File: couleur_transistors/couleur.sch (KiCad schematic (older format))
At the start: 20 parts, among them P1 CONN_02X03, P2 Mounting, P3 Mounting, P4 Mounting, P5 Mounting, U1 S4282-51

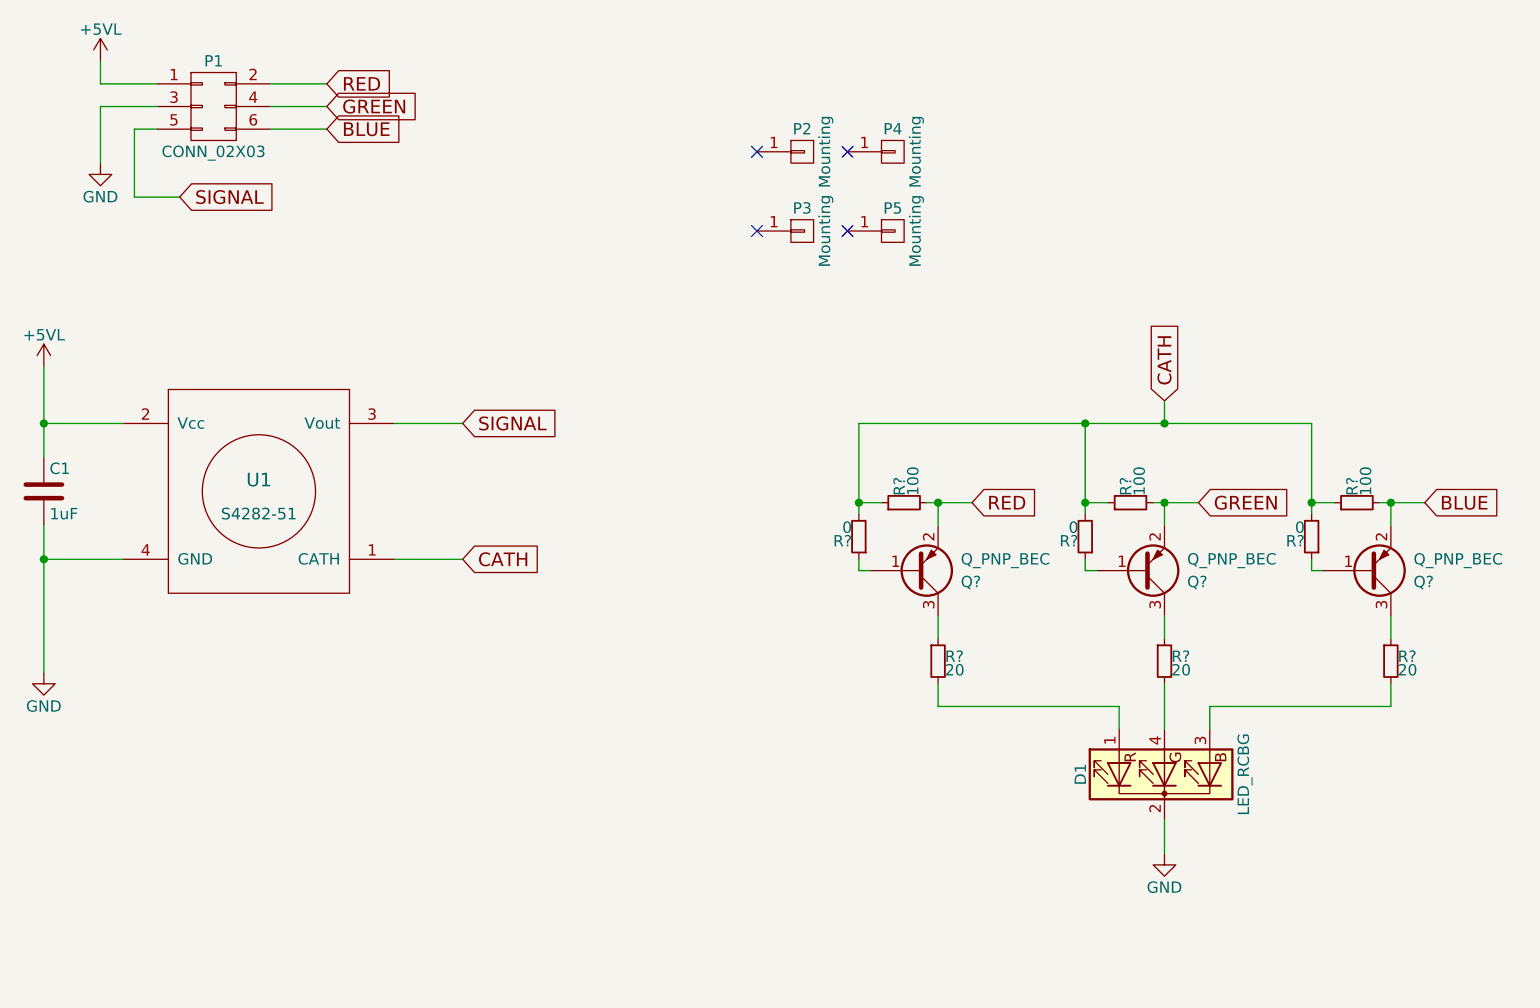
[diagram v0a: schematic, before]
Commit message: COuleur avec transistors
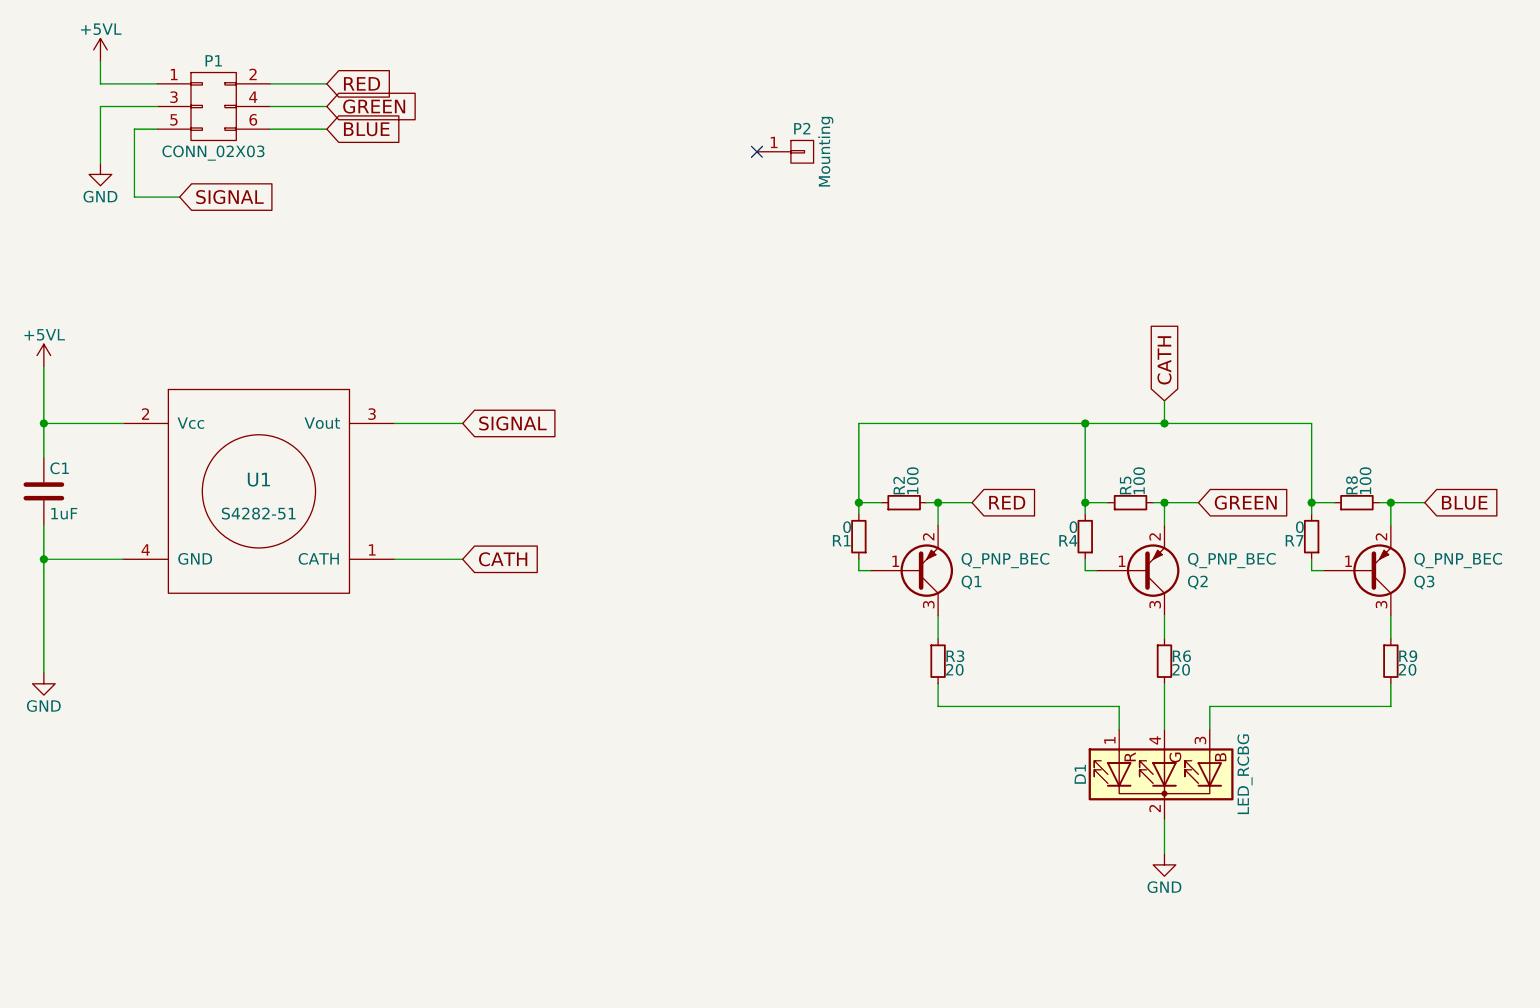
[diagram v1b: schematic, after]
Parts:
- removed P3, P4, P5: Mounting, Mounting_Holes:MountingHole_3.2mm_M3_Pad, symbol CONN_01X01
- Q1, Q2, Q3: renamed from Q?; footprint (none) -> TO_SOT_Packages_SMD:SOT-23
- R1, R2, R3, R4, R5, R6, R7, R8, R9: renamed from R?; footprint (none) -> Resistors_SMD:R_0603_HandSoldering
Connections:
- no-connect marks 4 -> 1
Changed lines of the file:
@@
 $EndComp
 $Comp
-L GND #PWR2
+L GND #PWR01
 U 1 1 5A77312B
 P 3550 4800
-F 0 "#PWR2" H 3550 4550 50  0001 C CNN
+F 0 "#PWR01" H 3550 4550 50  0001 C CNN
 F 1 "GND" H 3550 4650 50  0000 C CNN
 F 2 "" H 3550 4800 50  0000 C CNN
@@
 $EndComp
 $Comp
-L +5VL #PWR1
+L +5VL #PWR02
 U 1 1 5A773143
 P 3550 3450
-F 0 "#PWR1" H 3550 3300 50  0001 C CNN
+F 0 "#PWR02" H 3550 3300 50  0001 C CNN
 F 1 "+5VL" H 3550 3590 50  0000 C CNN
 F 2 "" H 3550 3450 50  0000 C CNN
@@
 $EndComp
 Wire Wire Line
-	3550 3450 3550 3700
-Wire Wire Line
-	3550 3700 3550 3850
+	3550 3450 3550 3850
 Wire Wire Line
 	3550 3700 3900 3700
@@
 	3900 4300 3550 4300
 Wire Wire Line
-	3550 4150 3550 4300
-Wire Wire Line
-	3550 4300 3550 4800
-$Comp
-L +5VL #PWR3
+	3550 4150 3550 4800
+$Comp
+L +5VL #PWR03
 U 1 1 5A773165
 P 3800 2100
-F 0 "#PWR3" H 3800 1950 50  0001 C CNN
+F 0 "#PWR03" H 3800 1950 50  0001 C CNN
 F 1 "+5VL" H 3800 2240 50  0000 C CNN
 F 2 "" H 3800 2100 50  0000 C CNN
@@
 $EndComp
 $Comp
-L GND #PWR4
+L GND #PWR04
 U 1 1 5A773176
 P 3800 2550
-F 0 "#PWR4" H 3800 2300 50  0001 C CNN
+F 0 "#PWR04" H 3800 2300 50  0001 C CNN
 F 1 "GND" H 3800 2400 50  0000 C CNN
 F 2 "" H 3800 2550 50  0000 C CNN
@@
 $EndComp
 NoConn ~ 6700 2500
-$Comp
-L CONN_01X01 P3
-U 1 1 5A7B0BC5
-P 6900 2850
-F 0 "P3" H 6900 2950 50  0000 C CNN
-F 1 "Mounting" V 7000 2850 50  0000 C CNN
-F 2 "Mounting_Holes:MountingHole_3.2mm_M3_Pad" H 6900 2850 50  0001 C CNN
-F 3 "" H 6900 2850 50  0000 C CNN
-	1    6900 2850
-	1    0    0    -1
-$EndComp
-NoConn ~ 6700 2850
-$Comp
-L CONN_01X01 P4
-U 1 1 5A7B0C29
-P 7300 2500
-F 0 "P4" H 7300 2600 50  0000 C CNN
-F 1 "Mounting" V 7400 2500 50  0000 C CNN
-F 2 "Mounting_Holes:MountingHole_3.2mm_M3_Pad" H 7300 2500 50  0001 C CNN
-F 3 "" H 7300 2500 50  0000 C CNN
-	1    7300 2500
-	1    0    0    -1
-$EndComp
-$Comp
-L CONN_01X01 P5
-U 1 1 5A7B0CFA
-P 7300 2850
-F 0 "P5" H 7300 2950 50  0000 C CNN
-F 1 "Mounting" V 7400 2850 50  0000 C CNN
-F 2 "Mounting_Holes:MountingHole_3.2mm_M3_Pad" H 7300 2850 50  0001 C CNN
-F 3 "" H 7300 2850 50  0000 C CNN
-	1    7300 2850
-	1    0    0    -1
-$EndComp
-NoConn ~ 7100 2500
-NoConn ~ 7100 2850
 $Comp
 L LED_RCBG D1
@@
 $EndComp
 $Comp
-L GND #PWR?
+L GND #PWR05
 U 1 1 5A7A0A21
 P 8500 5600
-F 0 "#PWR?" H 8500 5350 50  0001 C CNN
+F 0 "#PWR05" H 8500 5350 50  0001 C CNN
 F 1 "GND" H 8500 5450 50  0000 C CNN
 F 2 "" H 8500 5600 50  0000 C CNN
@@
 	8500 5450 8500 5600
 $Comp
-L Q_PNP_BEC Q?
+L Q_PNP_BEC Q1
 U 1 1 5A7A0A6A
 P 7400 4350
-F 0 "Q?" H 7600 4400 50  0000 L CNN
+F 0 "Q1" H 7600 4400 50  0000 L CNN
 F 1 "Q_PNP_BEC" H 7600 4300 50  0000 L CNN
-F 2 "" H 7600 4450 50  0000 C CNN
+F 2 "TO_SOT_Packages_SMD:SOT-23" H 7600 4450 50  0001 C CNN
 F 3 "" H 7400 4350 50  0000 C CNN
 	1    7400 4350
@@
 $EndComp
 $Comp
-L R_Small R?
+L R_Small R3
 U 1 1 5A7A0C40
 P 7500 4750
-F 0 "R?" H 7530 4770 50  0000 L CNN
+F 0 "R3" H 7530 4770 50  0000 L CNN
 F 1 "20" H 7530 4710 50  0000 L CNN
-F 2 "" H 7500 4750 50  0000 C CNN
+F 2 "Resistors_SMD:R_0603_HandSoldering" H 7500 4750 50  0001 C CNN
 F 3 "" H 7500 4750 50  0000 C CNN
 	1    7500 4750
@@
 $EndComp
 $Comp
-L R_Small R?
+L R_Small R6
 U 1 1 5A7A0C7B
 P 8500 4750
-F 0 "R?" H 8530 4770 50  0000 L CNN
+F 0 "R6" H 8530 4770 50  0000 L CNN
 F 1 "20" H 8530 4710 50  0000 L CNN
-F 2 "" H 8500 4750 50  0000 C CNN
+F 2 "Resistors_SMD:R_0603_HandSoldering" H 8500 4750 50  0001 C CNN
 F 3 "" H 8500 4750 50  0000 C CNN
 	1    8500 4750
@@
 $EndComp
 $Comp
-L R_Small R?
+L R_Small R9
 U 1 1 5A7A0CB2
 P 9500 4750
-F 0 "R?" H 9530 4770 50  0000 L CNN
+F 0 "R9" H 9530 4770 50  0000 L CNN
 F 1 "20" H 9530 4710 50  0000 L CNN
-F 2 "" H 9500 4750 50  0000 C CNN
+F 2 "Resistors_SMD:R_0603_HandSoldering" H 9500 4750 50  0001 C CNN
 F 3 "" H 9500 4750 50  0000 C CNN
 	1    9500 4750
@@
 $EndComp
 $Comp
-L R_Small R?
+L R_Small R1
 U 1 1 5A7A0CF2
 P 7150 4200
-F 0 "R?" H 7180 4220 50  0000 L CNN
+F 0 "R1" H 7180 4220 50  0000 L CNN
 F 1 "0" H 7180 4160 50  0000 L CNN
-F 2 "" H 7150 4200 50  0000 C CNN
+F 2 "Resistors_SMD:R_0603_HandSoldering" H 7150 4200 50  0001 C CNN
 F 3 "" H 7150 4200 50  0000 C CNN
 	1    7150 4200
@@
 $EndComp
 $Comp
-L R_Small R?
+L R_Small R2
 U 1 1 5A7A0D69
 P 7350 4050
-F 0 "R?" H 7380 4070 50  0000 L CNN
+F 0 "R2" H 7380 4070 50  0000 L CNN
 F 1 "100" H 7380 4010 50  0000 L CNN
-F 2 "" H 7350 4050 50  0000 C CNN
+F 2 "Resistors_SMD:R_0603_HandSoldering" H 7350 4050 50  0001 C CNN
 F 3 "" H 7350 4050 50  0000 C CNN
 	1    7350 4050
@@
 	7500 4150 7500 4050
 Wire Wire Line
-	7450 4050 7500 4050
-Wire Wire Line
-	7500 4050 7650 4050
+	7450 4050 7650 4050
 Wire Wire Line
 	7250 4050 7150 4050
@@
 CATH
 $Comp
-L R_Small R?
+L R_Small R4
 U 1 1 5A7A1702
 P 8150 4200
-F 0 "R?" H 8180 4220 50  0000 L CNN
+F 0 "R4" H 8180 4220 50  0000 L CNN
 F 1 "0" H 8180 4160 50  0000 L CNN
-F 2 "" H 8150 4200 50  0000 C CNN
+F 2 "Resistors_SMD:R_0603_HandSoldering" H 8150 4200 50  0001 C CNN
 F 3 "" H 8150 4200 50  0000 C CNN
 	1    8150 4200
@@
 $EndComp
 Wire Wire Line
-	8150 3700 8150 4050
-Wire Wire Line
-	8150 4050 8150 4100
-$Comp
-L R_Small R?
+	8150 3700 8150 4100
+$Comp
+L R_Small R5
 U 1 1 5A7A184F
 P 8350 4050
-F 0 "R?" H 8380 4070 50  0000 L CNN
+F 0 "R5" H 8380 4070 50  0000 L CNN
 F 1 "100" H 8380 4010 50  0000 L CNN
-F 2 "" H 8350 4050 50  0000 C CNN
+F 2 "Resistors_SMD:R_0603_HandSoldering" H 8350 4050 50  0001 C CNN
 F 3 "" H 8350 4050 50  0000 C CNN
 	1    8350 4050
@@
 Connection ~ 8150 4050
 $Comp
-L Q_PNP_BEC Q?
+L Q_PNP_BEC Q2
 U 1 1 5A7A18E8
 P 8400 4350
-F 0 "Q?" H 8600 4400 50  0000 L CNN
+F 0 "Q2" H 8600 4400 50  0000 L CNN
 F 1 "Q_PNP_BEC" H 8600 4300 50  0000 L CNN
-F 2 "" H 8600 4450 50  0000 C CNN
+F 2 "TO_SOT_Packages_SMD:SOT-23" H 8600 4450 50  0001 C CNN
 F 3 "" H 8400 4350 50  0000 C CNN
 	1    8400 4350
@@
 	8150 4350 8200 4350
 Wire Wire Line
-	8450 4050 8500 4050
-Wire Wire Line
-	8500 4050 8650 4050
+	8450 4050 8650 4050
 Wire Wire Line
 	8500 4050 8500 4150
@@
 	8500 4550 8500 4650
 Wire Wire Line
-	7150 3700 7150 4050
-Wire Wire Line
-	7150 4050 7150 4100
-Wire Wire Line
-	7150 3700 8150 3700
-Wire Wire Line
-	8150 3700 8500 3700
-Wire Wire Line
-	8500 3700 9150 3700
+	7150 3700 7150 4100
+Wire Wire Line
+	7150 3700 9150 3700
 Wire Wire Line
 	8500 3700 8500 3600
@@
 Connection ~ 8150 3700
 $Comp
-L R_Small R?
+L R_Small R7
 U 1 1 5A7A1EB9
 P 9150 4200
-F 0 "R?" H 9180 4220 50  0000 L CNN
+F 0 "R7" H 9180 4220 50  0000 L CNN
 F 1 "0" H 9180 4160 50  0000 L CNN
-F 2 "" H 9150 4200 50  0000 C CNN
+F 2 "Resistors_SMD:R_0603_HandSoldering" H 9150 4200 50  0001 C CNN
 F 3 "" H 9150 4200 50  0000 C CNN
 	1    9150 4200
@@
 $EndComp
 $Comp
-L R_Small R?
+L R_Small R8
 U 1 1 5A7A1F6E
 P 9350 4050
-F 0 "R?" H 9380 4070 50  0000 L CNN
+F 0 "R8" H 9380 4070 50  0000 L CNN
 F 1 "100" H 9380 4010 50  0000 L CNN
-F 2 "" H 9350 4050 50  0000 C CNN
+F 2 "Resistors_SMD:R_0603_HandSoldering" H 9350 4050 50  0001 C CNN
 F 3 "" H 9350 4050 50  0000 C CNN
 	1    9350 4050
@@
 $EndComp
 Wire Wire Line
-	9150 3700 9150 4050
-Wire Wire Line
-	9150 4050 9150 4100
+	9150 3700 9150 4100
 Wire Wire Line
 	9150 4050 9250 4050
@@
 Connection ~ 9150 4050
 $Comp
-L Q_PNP_BEC Q?
+L Q_PNP_BEC Q3
 U 1 1 5A7A20CB
 P 9400 4350
-F 0 "Q?" H 9600 4400 50  0000 L CNN
+F 0 "Q3" H 9600 4400 50  0000 L CNN
 F 1 "Q_PNP_BEC" H 9600 4300 50  0000 L CNN
-F 2 "" H 9600 4450 50  0000 C CNN
+F 2 "TO_SOT_Packages_SMD:SOT-23" H 9600 4450 50  0001 C CNN
 F 3 "" H 9400 4350 50  0000 C CNN
 	1    9400 4350
@@
 $EndComp
 Wire Wire Line
-	9450 4050 9500 4050
-Wire Wire Line
-	9500 4050 9650 4050
+	9450 4050 9650 4050
 Wire Wire Line
 	9500 4050 9500 4150

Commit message: Couleur
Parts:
- removed Q2, Q3: Q_PNP_BEC, TO_SOT_Packages_SMD:SOT-23, symbol Q_PNP_BEC
- removed R1, R4, R7: 0, Resistors_SMD:R_0603_HandSoldering, symbol R_Small
- removed R2, R5, R8: 100, Resistors_SMD:R_0603_HandSoldering, symbol R_Small
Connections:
- net BLUE: now also R9.1
- net CATH: now also Q1.1 (B)
- net GND: now also Q1.3 (C); no longer D1.2 (K)
- net GREEN: now also R6.1
- net RED: now also R3.1; no longer Q1.2 (E)
- new net: D1.2 (K), Q1.2 (E)
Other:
- moved on the sheet: Q1, R6
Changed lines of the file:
@@
 Wire Wire Line
 	5400 3700 5100 3700
-Text GLabel 7650 4050 2    60   Input ~ 0
+Text GLabel 7500 4550 1    60   Input ~ 0
 RED
-Text GLabel 8650 4050 2    60   Input ~ 0
+Text GLabel 8500 4550 1    60   Input ~ 0
 GREEN
-Text GLabel 9650 4050 2    60   Input ~ 0
+Text GLabel 9500 4550 1    60   Input ~ 0
 BLUE
 $Comp
@@
 L GND #PWR05
 U 1 1 5A7A0A21
-P 8500 5600
-F 0 "#PWR05" H 8500 5350 50  0001 C CNN
-F 1 "GND" H 8500 5450 50  0000 C CNN
-F 2 "" H 8500 5600 50  0000 C CNN
-F 3 "" H 8500 5600 50  0000 C CNN
-	1    8500 5600
+P 8500 6000
+F 0 "#PWR05" H 8500 5750 50  0001 C CNN
+F 1 "GND" H 8500 5850 50  0000 C CNN
+F 2 "" H 8500 6000 50  0000 C CNN
+F 3 "" H 8500 6000 50  0000 C CNN
+	1    8500 6000
 	1    0    0    -1
 $EndComp
-Wire Wire Line
-	8500 5450 8500 5600
 $Comp
 L Q_PNP_BEC Q1
 U 1 1 5A7A0A6A
-P 7400 4350
-F 0 "Q1" H 7600 4400 50  0000 L CNN
-F 1 "Q_PNP_BEC" H 7600 4300 50  0000 L CNN
-F 2 "TO_SOT_Packages_SMD:SOT-23" H 7600 4450 50  0001 C CNN
-F 3 "" H 7400 4350 50  0000 C CNN
-	1    7400 4350
+P 8400 5700
+F 0 "Q1" H 8600 5750 50  0000 L CNN
+F 1 "Q_PNP_BEC" H 8600 5650 50  0000 L CNN
+F 2 "TO_SOT_Packages_SMD:SOT-23" H 8600 5800 50  0001 C CNN
+F 3 "" H 8400 5700 50  0000 C CNN
+	1    8400 5700
 	1    0    0    1
 $EndComp
@@
 L R_Small R6
 U 1 1 5A7A0C7B
-P 8500 4750
-F 0 "R6" H 8530 4770 50  0000 L CNN
-F 1 "20" H 8530 4710 50  0000 L CNN
-F 2 "Resistors_SMD:R_0603_HandSoldering" H 8500 4750 50  0001 C CNN
-F 3 "" H 8500 4750 50  0000 C CNN
-	1    8500 4750
+P 8500 4850
+F 0 "R6" H 8530 4870 50  0000 L CNN
+F 1 "20" H 8530 4810 50  0000 L CNN
+F 2 "Resistors_SMD:R_0603_HandSoldering" H 8500 4850 50  0001 C CNN
+F 3 "" H 8500 4850 50  0000 C CNN
+	1    8500 4850
 	1    0    0    -1
 $EndComp
@@
 	1    0    0    -1
 $EndComp
-$Comp
-L R_Small R1
-U 1 1 5A7A0CF2
-P 7150 4200
-F 0 "R1" H 7180 4220 50  0000 L CNN
-F 1 "0" H 7180 4160 50  0000 L CNN
-F 2 "Resistors_SMD:R_0603_HandSoldering" H 7150 4200 50  0001 C CNN
-F 3 "" H 7150 4200 50  0000 C CNN
-	1    7150 4200
-	-1   0    0    1
-$EndComp
-$Comp
-L R_Small R2
-U 1 1 5A7A0D69
-P 7350 4050
-F 0 "R2" H 7380 4070 50  0000 L CNN
-F 1 "100" H 7380 4010 50  0000 L CNN
-F 2 "Resistors_SMD:R_0603_HandSoldering" H 7350 4050 50  0001 C CNN
-F 3 "" H 7350 4050 50  0000 C CNN
-	1    7350 4050
-	0    -1   -1   0
-$EndComp
 Text GLabel 5400 4300 2    60   Input ~ 0
 CATH
-Wire Wire Line
-	7200 4350 7150 4350
-Wire Wire Line
-	7150 4350 7150 4300
-Wire Wire Line
-	7500 4150 7500 4050
-Wire Wire Line
-	7450 4050 7650 4050
-Wire Wire Line
-	7250 4050 7150 4050
-Connection ~ 7500 4050
 Wire Wire Line
 	7500 4550 7500 4650
 Wire Wire Line
 	7500 4850 7500 4950
-Text GLabel 8500 3600 1    60   Input ~ 0
+Text GLabel 8200 5700 0    60   Input ~ 0
 CATH
-$Comp
-L R_Small R4
-U 1 1 5A7A1702
-P 8150 4200
-F 0 "R4" H 8180 4220 50  0000 L CNN
-F 1 "0" H 8180 4160 50  0000 L CNN
-F 2 "Resistors_SMD:R_0603_HandSoldering" H 8150 4200 50  0001 C CNN
-F 3 "" H 8150 4200 50  0000 C CNN
-	1    8150 4200
-	-1   0    0    1
-$EndComp
 Wire Wire Line
-	8150 3700 8150 4100
-$Comp
-L R_Small R5
-U 1 1 5A7A184F
-P 8350 4050
-F 0 "R5" H 8380 4070 50  0000 L CNN
-F 1 "100" H 8380 4010 50  0000 L CNN
-F 2 "Resistors_SMD:R_0603_HandSoldering" H 8350 4050 50  0001 C CNN
-F 3 "" H 8350 4050 50  0000 C CNN
-	1    8350 4050
-	0    -1   -1   0
-$EndComp
-Wire Wire Line
-	8250 4050 8150 4050
-Connection ~ 8150 4050
-$Comp
-L Q_PNP_BEC Q2
-U 1 1 5A7A18E8
-P 8400 4350
-F 0 "Q2" H 8600 4400 50  0000 L CNN
-F 1 "Q_PNP_BEC" H 8600 4300 50  0000 L CNN
-F 2 "TO_SOT_Packages_SMD:SOT-23" H 8600 4450 50  0001 C CNN
-F 3 "" H 8400 4350 50  0000 C CNN
-	1    8400 4350
-	1    0    0    1
-$EndComp
-Wire Wire Line
-	8150 4300 8150 4350
-Wire Wire Line
-	8150 4350 8200 4350
-Wire Wire Line
-	8450 4050 8650 4050
-Wire Wire Line
-	8500 4050 8500 4150
-Connection ~ 8500 4050
-Wire Wire Line
-	8500 4550 8500 4650
-Wire Wire Line
-	7150 3700 7150 4100
-Wire Wire Line
-	7150 3700 9150 3700
-Wire Wire Line
-	8500 3700 8500 3600
-Connection ~ 7150 4050
-Connection ~ 8150 3700
-$Comp
-L R_Small R7
-U 1 1 5A7A1EB9
-P 9150 4200
-F 0 "R7" H 9180 4220 50  0000 L CNN
-F 1 "0" H 9180 4160 50  0000 L CNN
-F 2 "Resistors_SMD:R_0603_HandSoldering" H 9150 4200 50  0001 C CNN
-F 3 "" H 9150 4200 50  0000 C CNN
-	1    9150 4200
-	-1   0    0    1
-$EndComp
-$Comp
-L R_Small R8
-U 1 1 5A7A1F6E
-P 9350 4050
-F 0 "R8" H 9380 4070 50  0000 L CNN
-F 1 "100" H 9380 4010 50  0000 L CNN
-F 2 "Resistors_SMD:R_0603_HandSoldering" H 9350 4050 50  0001 C CNN
-F 3 "" H 9350 4050 50  0000 C CNN
-	1    9350 4050
-	0    -1   -1   0
-$EndComp
-Wire Wire Line
-	9150 3700 9150 4100
-Wire Wire Line
-	9150 4050 9250 4050
-Connection ~ 8500 3700
-Connection ~ 9150 4050
-$Comp
-L Q_PNP_BEC Q3
-U 1 1 5A7A20CB
-P 9400 4350
-F 0 "Q3" H 9600 4400 50  0000 L CNN
-F 1 "Q_PNP_BEC" H 9600 4300 50  0000 L CNN
-F 2 "TO_SOT_Packages_SMD:SOT-23" H 9600 4450 50  0001 C CNN
-F 3 "" H 9400 4350 50  0000 C CNN
-	1    9400 4350
-	1    0    0    1
-$EndComp
-Wire Wire Line
-	9450 4050 9650 4050
-Wire Wire Line
-	9500 4050 9500 4150
-Wire Wire Line
-	9200 4350 9150 4350
-Wire Wire Line
-	9150 4350 9150 4300
-Connection ~ 9500 4050
+	8500 4550 8500 4750
 Wire Wire Line
 	9500 4550 9500 4650
@@
 	8300 4950 8300 5050
 Wire Wire Line
-	8500 4850 8500 5050
+	8500 4950 8500 5050
 Wire Wire Line
 	9500 4850 9500 4950
@@
 Wire Wire Line
 	8700 4950 8700 5050
+Wire Wire Line
+	8500 5450 8500 5500
+Wire Wire Line
+	8500 5900 8500 6000
 $EndSCHEMATC

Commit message: maj
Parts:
- removed Q1: Q_PNP_BEC, TO_SOT_Packages_SMD:SOT-23, symbol Q_PNP_BEC
- removed R6, R9: 20, Resistors_SMD:R_0603_HandSoldering, symbol R_Small
- added C2, C3, C4, C5: 1uF, Capacitors_SMD:C_0603_HandSoldering, symbol C
- added R1, R2: 20, Resistors_SMD:R_0603_HandSoldering, symbol R_Small
- added U2, U3: NLAS2066, Housings_SSOP:TSSOP-8_3x3mm_Pitch0.65mm, symbol NLAS2066
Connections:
- wire segments 28 -> 57
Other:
- moved on the sheet: D1
